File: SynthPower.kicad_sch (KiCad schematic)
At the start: 27 parts, among them J9 Jack-DC, U1 TPS560200, U2 BUF634AIDDAR, U3 LM1117MP-3.3

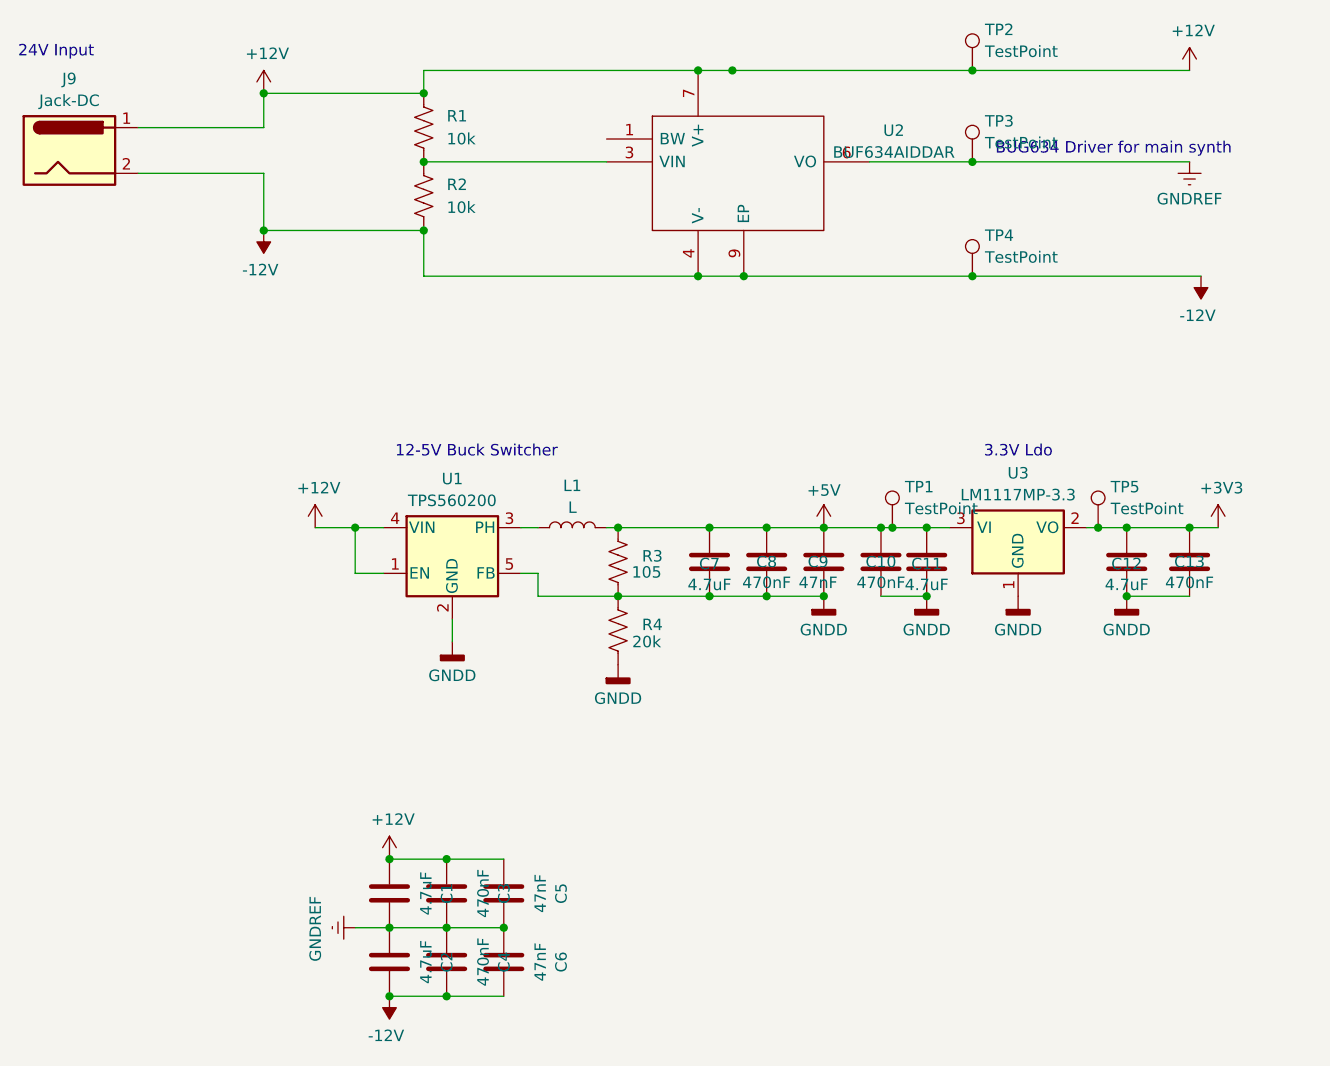
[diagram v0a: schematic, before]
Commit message: created pcb file, placed parts
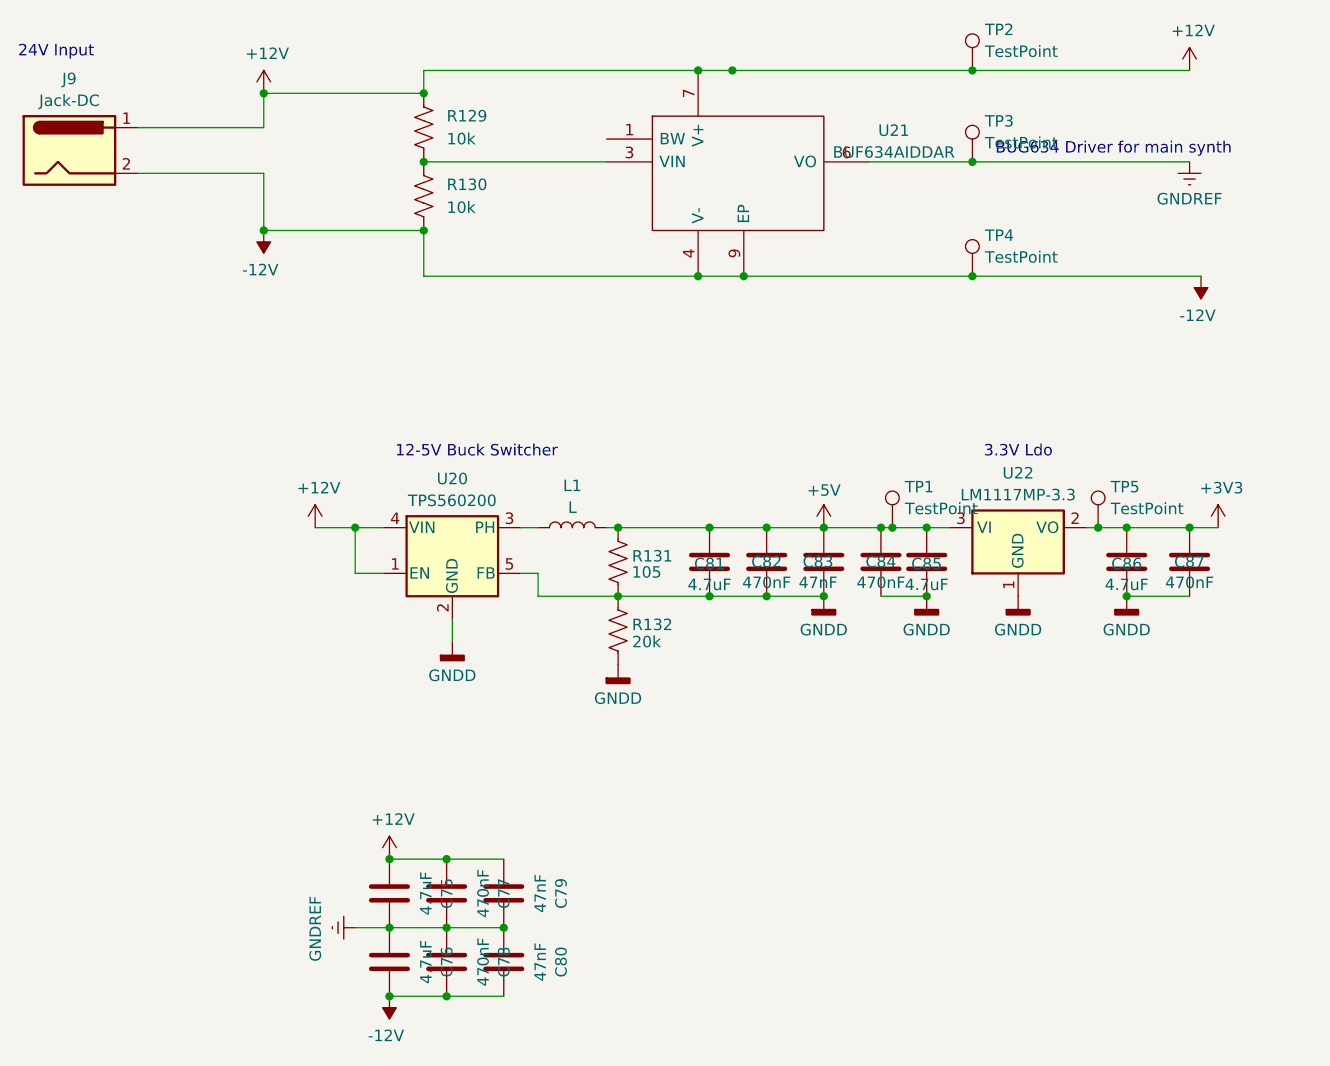
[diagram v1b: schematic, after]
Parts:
- renumbered C1 to C75, C2 to C76, C3 to C77, C4 to C78, C5 to C79, C6 to C80, C7 to C81, C8 to C82, C9 to C83, C10 to C84, C11 to C85, C12 to C86, C13 to C87, R1 to R129, R2 to R130, R3 to R131, R4 to R132, U1 to U20, U2 to U21, U3 to U22
